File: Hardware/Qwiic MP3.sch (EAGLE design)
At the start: 53 parts, among them J1 MICRO-SD, J3 PTH, J7 ISP, J8 3.5mm Audio, J9 Poke-Home, U1 TPA2005D1, U2 WT2003S, U3 AP2112-3.3V, U4 ATTINY84-ARDUINO

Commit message: Nearing production code
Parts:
- C3, C6: value 10uF -> 0.22uF; device SparkFun-Capacitors:10UF-0603-6.3V-20% -> SparkFun-Capacitors:0.22UF-0603-25V-10%
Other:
- note added: "7-Bit Unshifted I2C Address Open Jumper (Default): 0x37 Closed Jumper: 0x38 Software configurable as well"
- note removed: "7-bit unshifted I2C address: 0x60"
- note removed: "Don't drive INT high, just low (open drain)"
- note removed: "I2C Address Selection Open Jumper (Default): 0x37 Closed Jumper: 0x38"
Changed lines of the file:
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@@
 <part name="U$30" library="SparkFun-PowerSymbols" deviceset="5V" device=""/>
 <part name="SUPPLY1" library="SparkFun-PowerSymbols" deviceset="3.3V" device=""/>
-<part name="C3" library="SparkFun-Capacitors" deviceset="10UF" device="-0603-6.3V-20%" value="10uF"/>
-<part name="C6" library="SparkFun-Capacitors" deviceset="10UF" device="-0603-6.3V-20%" value="10uF"/>
+<part name="C3" library="SparkFun-Capacitors" deviceset="0.22UF" device="-0603-25V-10%" value="0.22uF"/>
+<part name="C6" library="SparkFun-Capacitors" deviceset="0.22UF" device="-0603-25V-10%" value="0.22uF"/>
 <part name="C9" library="SparkFun-Capacitors" deviceset="1.0UF-16V-10%(0603)" device="" value="1.0uF"/>
 <part name="SUPPLY20" library="SparkFun-PowerSymbols" deviceset="VCCIO" device=""/>
@@
 <text x="170.434" y="11.43" size="2.54" layer="94">N. Seidle</text>
 <text x="237.744" y="7.366" size="2.54" layer="94">X10</text>
-<text x="157.48" y="106.68" size="1.778" layer="97">7-bit unshifted I2C address: 0x60</text>
 <text x="74.803" y="75.311" size="1.778" layer="97" rot="R90">Power</text>
-<text x="156.718" y="99.06" size="1.778" layer="97">I2C Address Selection
+<text x="156.718" y="99.06" size="1.778" layer="97">7-Bit Unshifted I2C Address
 Open Jumper (Default): 0x37
-Closed Jumper: 0x38</text>
+Closed Jumper: 0x38
+Software configurable as well</text>
 <text x="215.773" y="164.211" size="1.778" layer="97">I2C Pull Ups</text>
-<text x="55.88" y="2.54" size="1.27" layer="91">Don't drive INT high, just low (open drain)</text>
 <text x="102.235" y="57.912" size="1.778" layer="97">Button Triggers</text>
 <text x="7.62" y="66.04" size="1.778" layer="97">3.3V VReg prevents USB 5V

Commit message: Small schematic note change
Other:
- note added: "7-Bit Unshifted I2C Address Open Jumper (Default): 0x37 Closed Jumper: 0x36 Software configurable as well"
- note removed: "7-Bit Unshifted I2C Address Open Jumper (Default): 0x37 Closed Jumper: 0x38 Software configurable as well"
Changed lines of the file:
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@@
 <text x="156.718" y="99.06" size="1.778" layer="97">7-Bit Unshifted I2C Address
 Open Jumper (Default): 0x37
-Closed Jumper: 0x38
+Closed Jumper: 0x36
 Software configurable as well</text>
 <text x="215.773" y="164.211" size="1.778" layer="97">I2C Pull Ups</text>

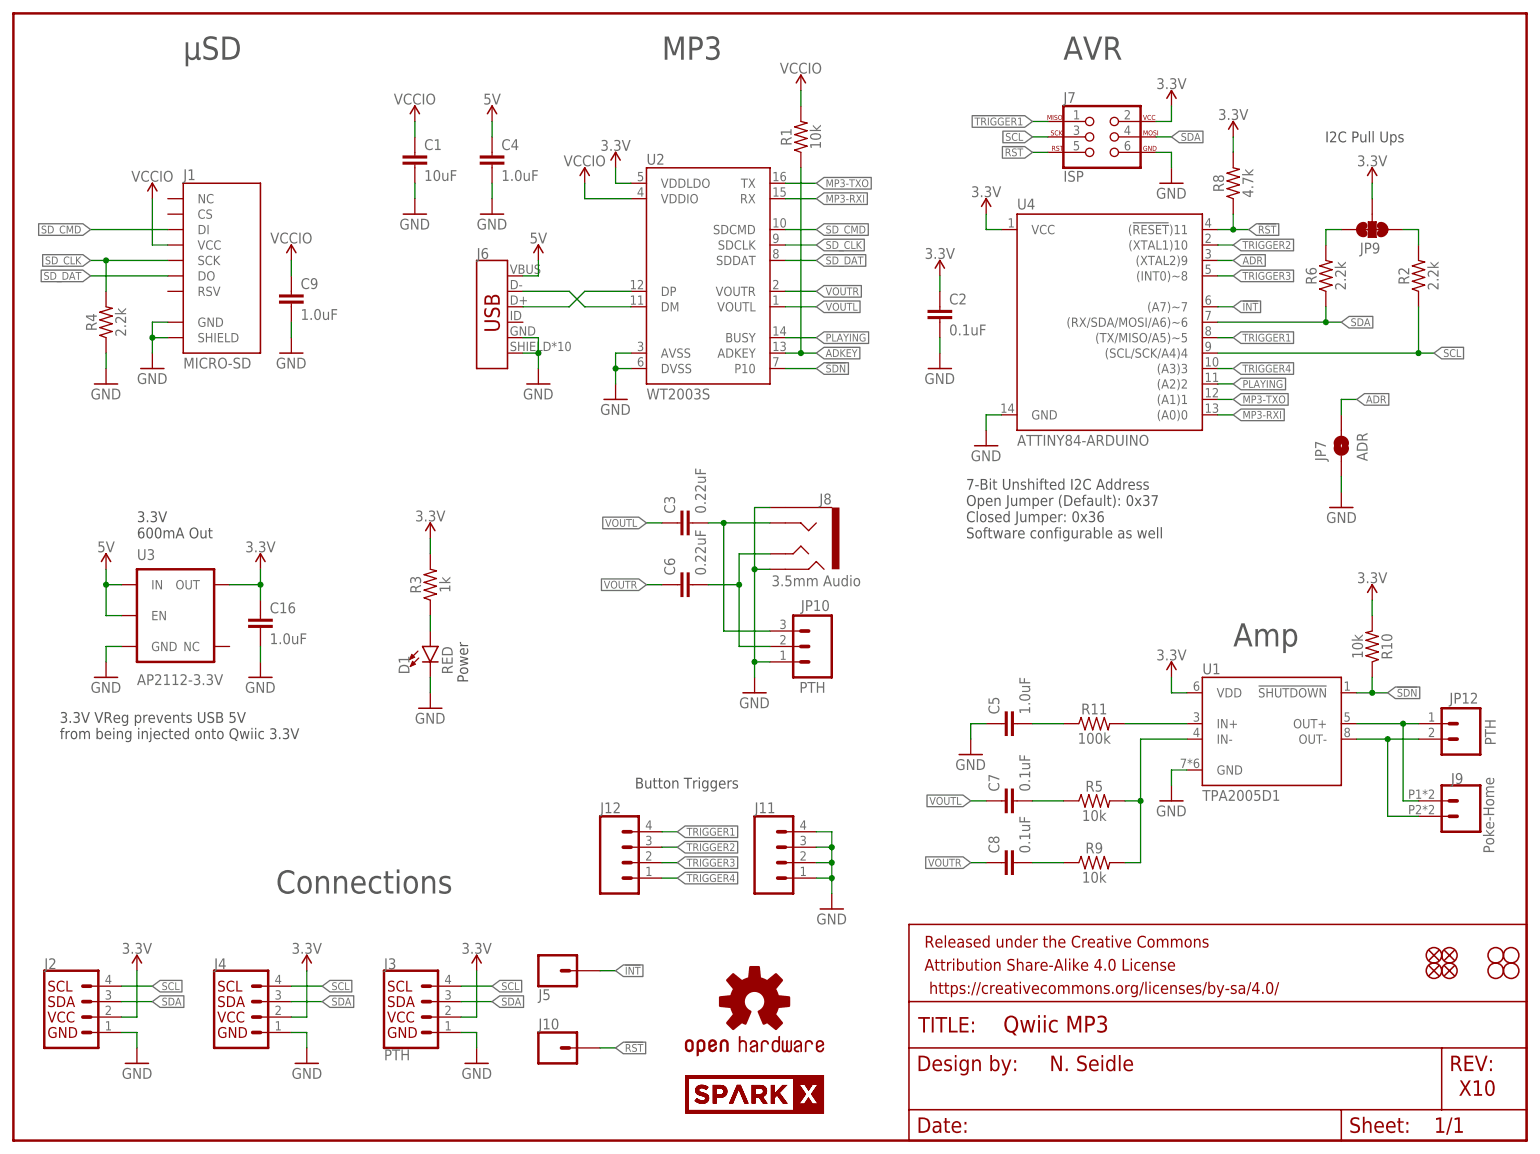
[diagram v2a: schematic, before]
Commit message: Update to USB C
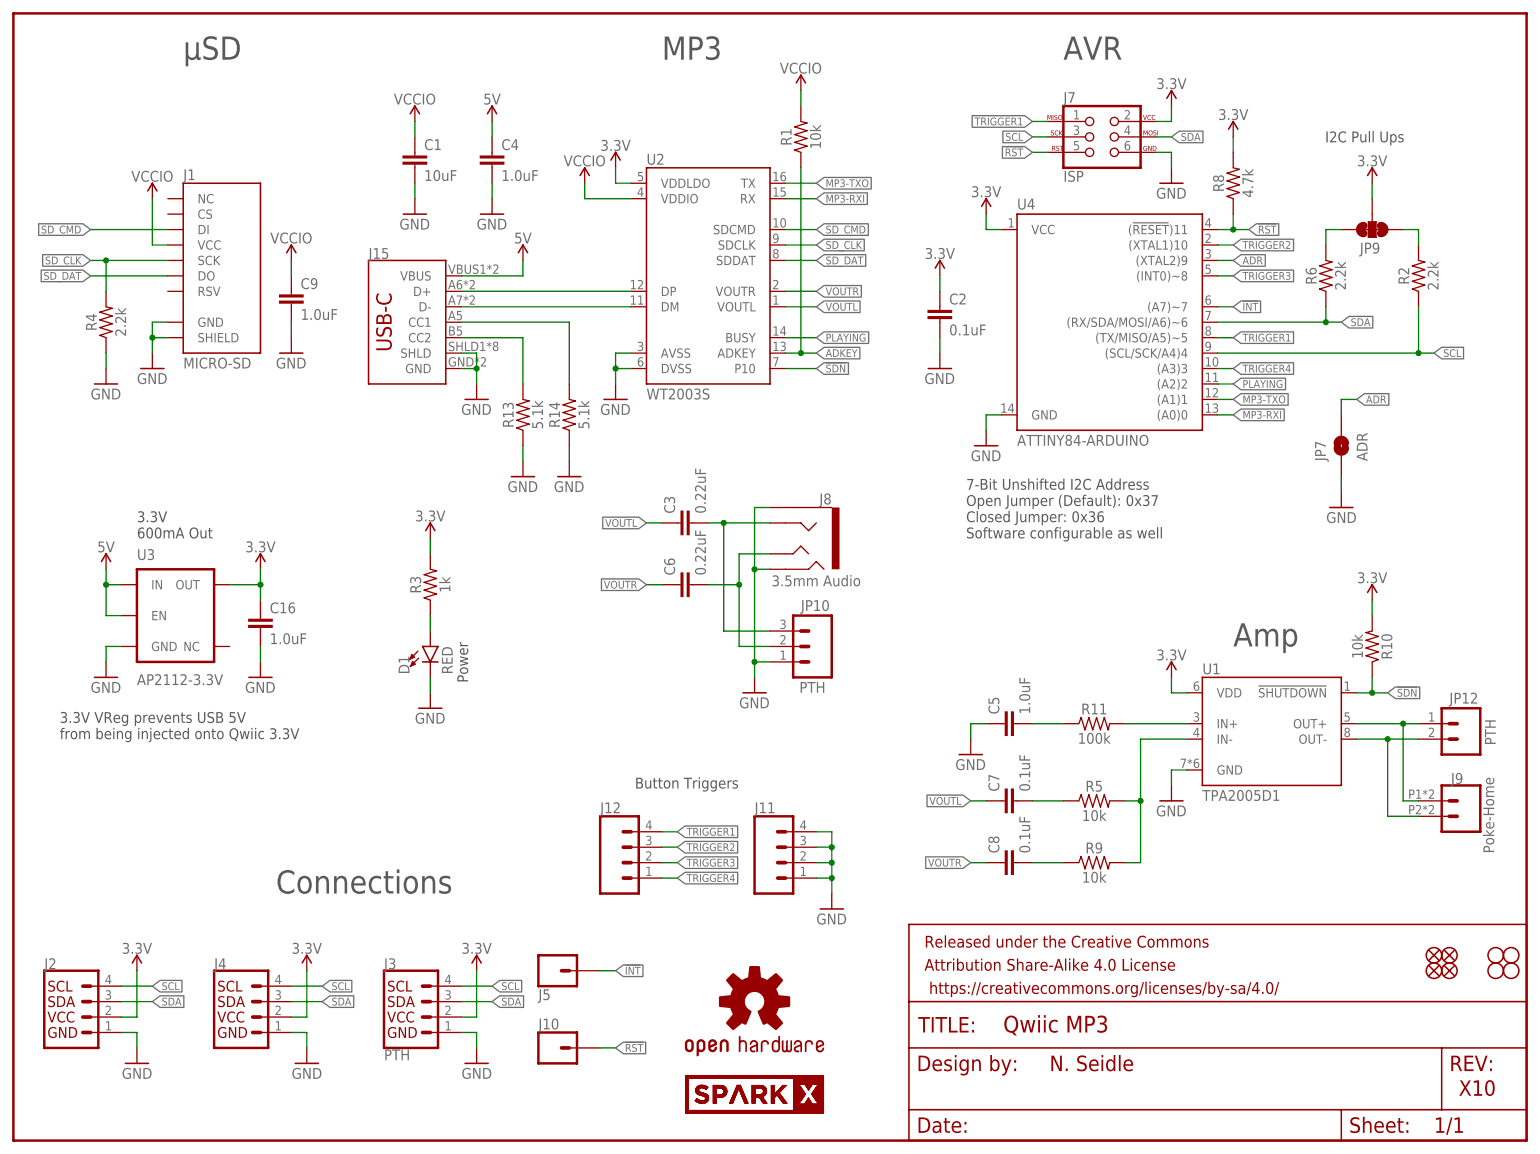
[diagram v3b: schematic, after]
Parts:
- removed J6: (no value), SparkFun-Connectors:USB_MICRO-B_HALF_PTH_MILL
- added J15: (no value), SparkFun-Connectors:USB_C16PIN
- added R13, R14: 5.1k, SparkFun-Resistors:5.1KOHM5.1KOHM-0603-1/10W-1%
- C16, C9: device SparkFun-Capacitors:1.0UF-16V-10%(0603) -> SparkFun-Capacitors:1.0UF-0603-16V-10%
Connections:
- new net N$1: J15.CC2, R13.2
- new net N$2: J15.CC1, R14.2
- net 5V: now also J15.VBUS; no longer J6.VBUS
- net D+: now also J15.D+; no longer J6.D+
- net D-: now also J15.D-; no longer J6.D-
- net GND: now also J15.GND, J15.SHLD, R13.1, R14.1; no longer J6.GND, J6.SHIELD
